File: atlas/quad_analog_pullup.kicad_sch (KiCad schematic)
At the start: 28 parts, among them U701 MCP6004, U702 SRV05-4, U703 NC7SB3157P6X, U704 NC7SB3157P6X

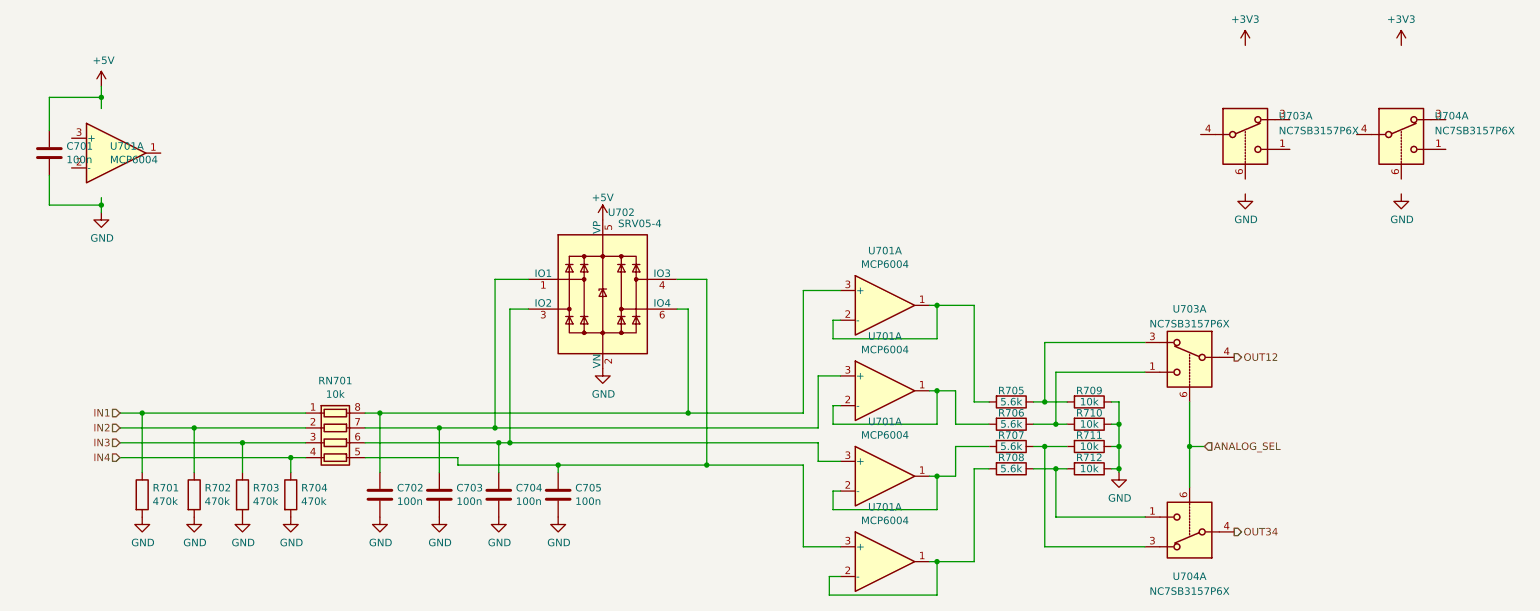
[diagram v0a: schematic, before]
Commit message: analog pullups
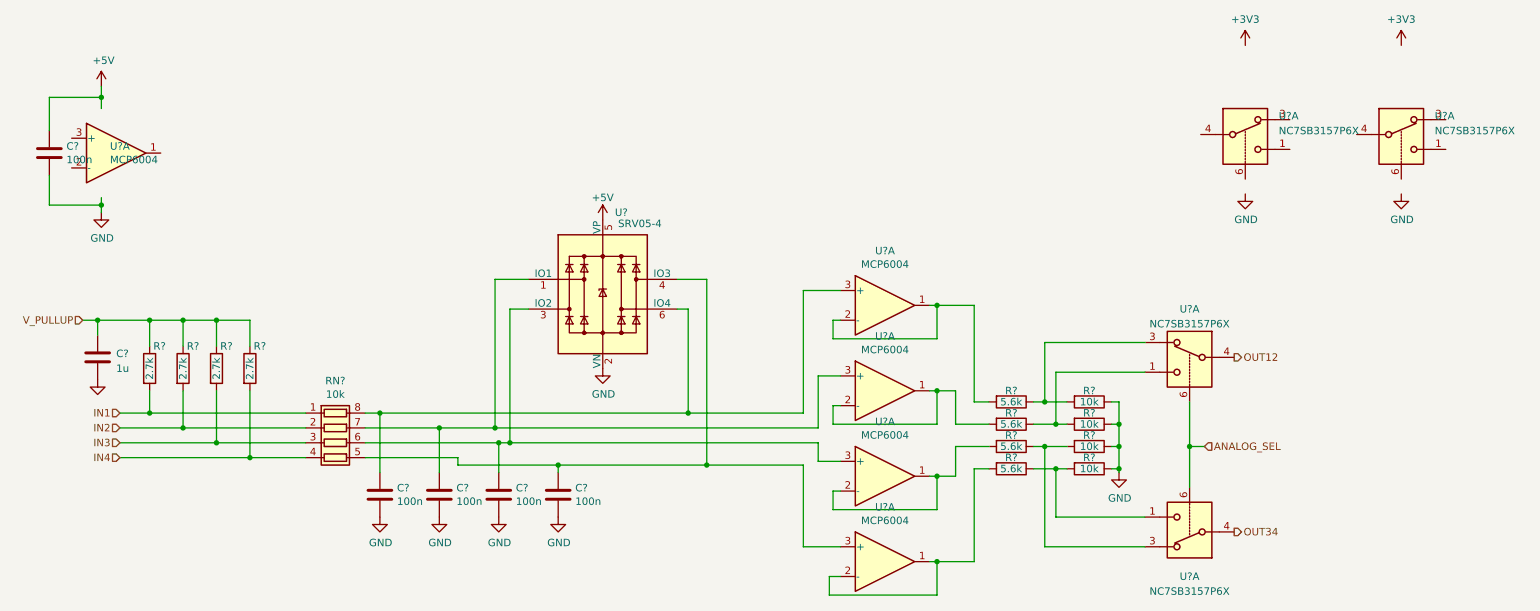
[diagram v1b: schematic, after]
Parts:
- removed C701: 100n, Capacitor_SMD:C_0603_1608Metric, symbol Device:C
- removed C702, C703, C704, C705: 100n, Capacitor_SMD:C_0402_1005Metric, symbol Device:C
- removed R701, R702, R703, R704: 470k, Resistor_SMD:R_0402_1005Metric, symbol Device:R
- removed R705, R706, R707, R708: 5.6k, Resistor_SMD:R_0402_1005Metric, symbol Device:R
- removed R709, R710, R711, R712: 10k, Resistor_SMD:R_0402_1005Metric, symbol Device:R
- removed RN701: 10k, Resistor_SMD:R_Array_Convex_4x0603, symbol Device:R_Pack04
- removed U701 (x5): MCP6004, Package_SO:TSSOP-14_4.4x5mm_P0.65mm, symbol Amplifier_Operational:MCP6004
- removed U702: SRV05-4, Package_TO_SOT_SMD:SOT-23-6, symbol Power_Protection:SRV05-4
- removed U703 (x2), U704 (x2): NC7SB3157P6X, Package_TO_SOT_SMD:SOT-363_SC-70-6, symbol Analog_Switch:NC7SB3157P6X
- added C?: 100n, Capacitor_SMD:C_0603_1608Metric, symbol Device:C
- added C? (x4): 100n, Capacitor_SMD:C_0402_1005Metric, symbol Device:C
- added C?: 1u, symbol Device:C
- added R? (x4): 10k, Resistor_SMD:R_0402_1005Metric, symbol Device:R
- added R? (x4): 2.7k, symbol Device:R
- added R? (x4): 5.6k, Resistor_SMD:R_0402_1005Metric, symbol Device:R
- added RN?: 10k, Resistor_SMD:R_Array_Convex_4x0603, symbol Device:R_Pack04
- added U? (x4): NC7SB3157P6X, Package_TO_SOT_SMD:SOT-363_SC-70-6, symbol Analog_Switch:NC7SB3157P6X
- added U?: SRV05-4, Package_TO_SOT_SMD:SOT-23-6, symbol Power_Protection:SRV05-4
- added U? (x5): MCP6004, Package_SO:TSSOP-14_4.4x5mm_P0.65mm, symbol Amplifier_Operational:MCP6004
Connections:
- net +5V: now also C?.1, U?.5 (VP)
- net ANALOG_SEL: now also U?.6, U?.6
- net GND: now also C?.2, C?.2, C?.2, C?.2, C?.2, C?.2, R?.1, R?.1, R?.1, R?.1, U?.2 (VN)
- net IN1: now also R?.2, RN?.1 (R1.1)
- net IN2: now also R?.2, RN?.2 (R2.1)
- net IN3: now also R?.2, RN?.3 (R3.1)
- net IN4: now also R?.2, RN?.4 (R4.1)
- net OUT12: now also U?.4
- net OUT34: now also U?.4
- new net: R?.1, R?.2, U?.1 (x2)
- new net: C?.1, RN?.5 (R4.2), U?.3 (+), U?.4 (IO3)
- new net: C?.1, RN?.6 (R3.2), U?.3 (+), U?.3 (IO2)
- new net: C?.1, RN?.7 (R2.2), U?.1 (IO1), U?.3 (+)
- new net: C?.1, RN?.8 (R1.2), U?.3 (+), U?.6 (IO4)
- new net: R?.1, R?.2, U?.3 (x2)
- new net: R?.2, U?.1, U?.2 (-) (x4)
- new net V_PULLUP: C?.1, R?.1, R?.1, R?.1, R?.1

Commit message: pin mapping
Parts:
- gave numbers to parts that had none: 23

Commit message: progressssss
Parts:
- removed C1101: 100n, Capacitor_SMD:C_0603_1608Metric, symbol Device:C
- removed C1102: 1u, symbol Device:C
- removed C1103, C1104, C1105, C1106: 100n, Capacitor_SMD:C_0402_1005Metric, symbol Device:C
- removed R1109, R1110, R1111, R1112: 10k, Resistor_SMD:R_0402_1005Metric, symbol Device:R
- removed RN1101: 10k, Resistor_SMD:R_Array_Convex_4x0603, symbol Device:R_Pack04
- removed U1101 (x5): MCP6004, Package_SO:TSSOP-14_4.4x5mm_P0.65mm, symbol Amplifier_Operational:MCP6004
- removed U1102: SRV05-4, Package_TO_SOT_SMD:SOT-23-6, symbol Power_Protection:SRV05-4
- removed U1103 (x2), U1104 (x2): NC7SB3157P6X, Package_TO_SOT_SMD:SOT-363_SC-70-6, symbol Analog_Switch:NC7SB3157P6X
- added Q1101, Q1104, Q1106, Q1108: 2N7002, Package_TO_SOT_SMD:SOT-23, symbol Device:Q_NMOS_GSD
- added Q1102 (x2), Q1103 (x2), Q1105 (x2), Q1107, Q1109: DMP2240UDM, Package_TO_SOT_SMD:SOT-23-6, symbol Device:Q_Dual_PMOS_G1S2G2D2S1D1
- R1101, R1103: value 2.7k -> 10k; footprint (none) -> Resistor_SMD:R_0603_1608Metric; LCSC (none) -> C25804
- R1102, R1104: footprint (none) -> Resistor_SMD:R_0603_1608Metric; LCSC (none) -> C13167
- R1105, R1107: value 5.6k -> 10k; footprint Resistor_SMD:R_0402_1005Metric -> Resistor_SMD:R_0603_1608Metric; LCSC C25908 -> C25804
- R1106, R1108: value 5.6k -> 2.7k; footprint Resistor_SMD:R_0402_1005Metric -> Resistor_SMD:R_0603_1608Metric; LCSC C25908 -> C13167
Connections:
- net GND: now also Q1101.2 (S), Q1104.2 (S), Q1106.2 (S), Q1108.2 (S)
- net IN1: now also R1102.2; no longer R1101.2
- net IN2: now also R1104.2; no longer R1102.2
- net IN3: now also R1106.2; no longer R1103.2
- net IN4: now also R1108.2; no longer R1104.2
- net V_PULLUP: now also Q1102.6 (D), Q1105.6 (D), Q1107.6 (D), Q1109.6 (D); no longer R1101.1, R1102.1, R1103.1, R1104.1
- net at R1106.1: now also Q1103.6 (D)
- net at R1107.1: now also Q1105.1 (G), Q1108.3 (D), Q1109.1 (G)
- net at R1108.1: now also Q1105.6 (D)
- net at R1107.2: now also Q1105.5 (S), Q1109.5 (S)
- net at R1105.1: now also Q1103.1 (G), Q1106.3 (D), Q1107.1 (G)
- net at R1105.2: now also Q1103.5 (S), Q1107.5 (S)
- new net: Q1101.3 (D), Q1102.1 (G), Q1103.1 (G), R1101.1
- new net: Q1102.5 (S), Q1103.5 (S), R1101.2
- new net: Q1102.6 (D), R1104.1
- new net: Q1102.1 (G), Q1104.3 (D), Q1105.1 (G), R1103.1
- new net: Q1102.5 (S), Q1105.5 (S), R1103.2
- new net: Q1103.6 (D), R1102.1
- new net PULL_EN_1: Q1101.1 (G)
- new net PULL_EN_2: Q1104.1 (G)
- new net PULL_EN_3: Q1106.1 (G)
- new net PULL_EN_4: Q1108.1 (G)
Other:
- added sheet QuadAnalog8 (quad_analog.kicad_sch)

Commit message: upgrade kicad
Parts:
- renumbered Q1101 to Q1001, Q1102 to Q1002, Q1103 to Q1002, Q1104 to Q1003, Q1105 to Q1004, Q1102 to Q1004, Q1106 to Q1005, Q1107 to Q1006, Q1103 to Q1006, Q1108 to Q1007, Q1105 to Q1008, Q1109 to Q1008, R1101 to R1001, R1102 to R1002, R1103 to R1003, R1104 to R1004, R1105 to R1005, R1106 to R1006, R1107 to R1007, R1108 to R1008
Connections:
- net at Q1007.3 (D), Q1008.1 (G), R1007.1: now also Q1008.3 (G); no longer Q1008.1 (G)
- net at Q1008.5 (S), R1007.2: now also Q1008.2 (S); no longer Q1008.5 (S)
- net at R1008.1: now also Q1008.4 (D); no longer Q1008.6 (D)
- net at Q1005.3 (D), Q1006.1 (G), R1005.1: now also Q1006.3 (G); no longer Q1006.1 (G)
- net at Q1006.5 (S), R1005.2: now also Q1006.2 (S); no longer Q1006.5 (S)
- net at R1006.1: now also Q1006.4 (D); no longer Q1006.6 (D)
- net at Q1001.3 (D), Q1002.1 (G), R1001.1: now also Q1002.3 (G); no longer Q1002.1 (G)
- net at Q1002.5 (S), R1001.2: now also Q1002.2 (S); no longer Q1002.5 (S)
- net at R1004.1: now also Q1004.4 (D); no longer Q1004.6 (D)
- net at Q1003.3 (D), Q1004.1 (G), R1003.1: now also Q1004.3 (G); no longer Q1004.1 (G)
- net at Q1004.5 (S), R1003.2: now also Q1004.2 (S); no longer Q1004.5 (S)
- net at R1002.1: now also Q1002.4 (D); no longer Q1002.6 (D)
